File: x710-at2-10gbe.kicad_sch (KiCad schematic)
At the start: 22 parts, among them U4 EZX710AT2_S_LMR5

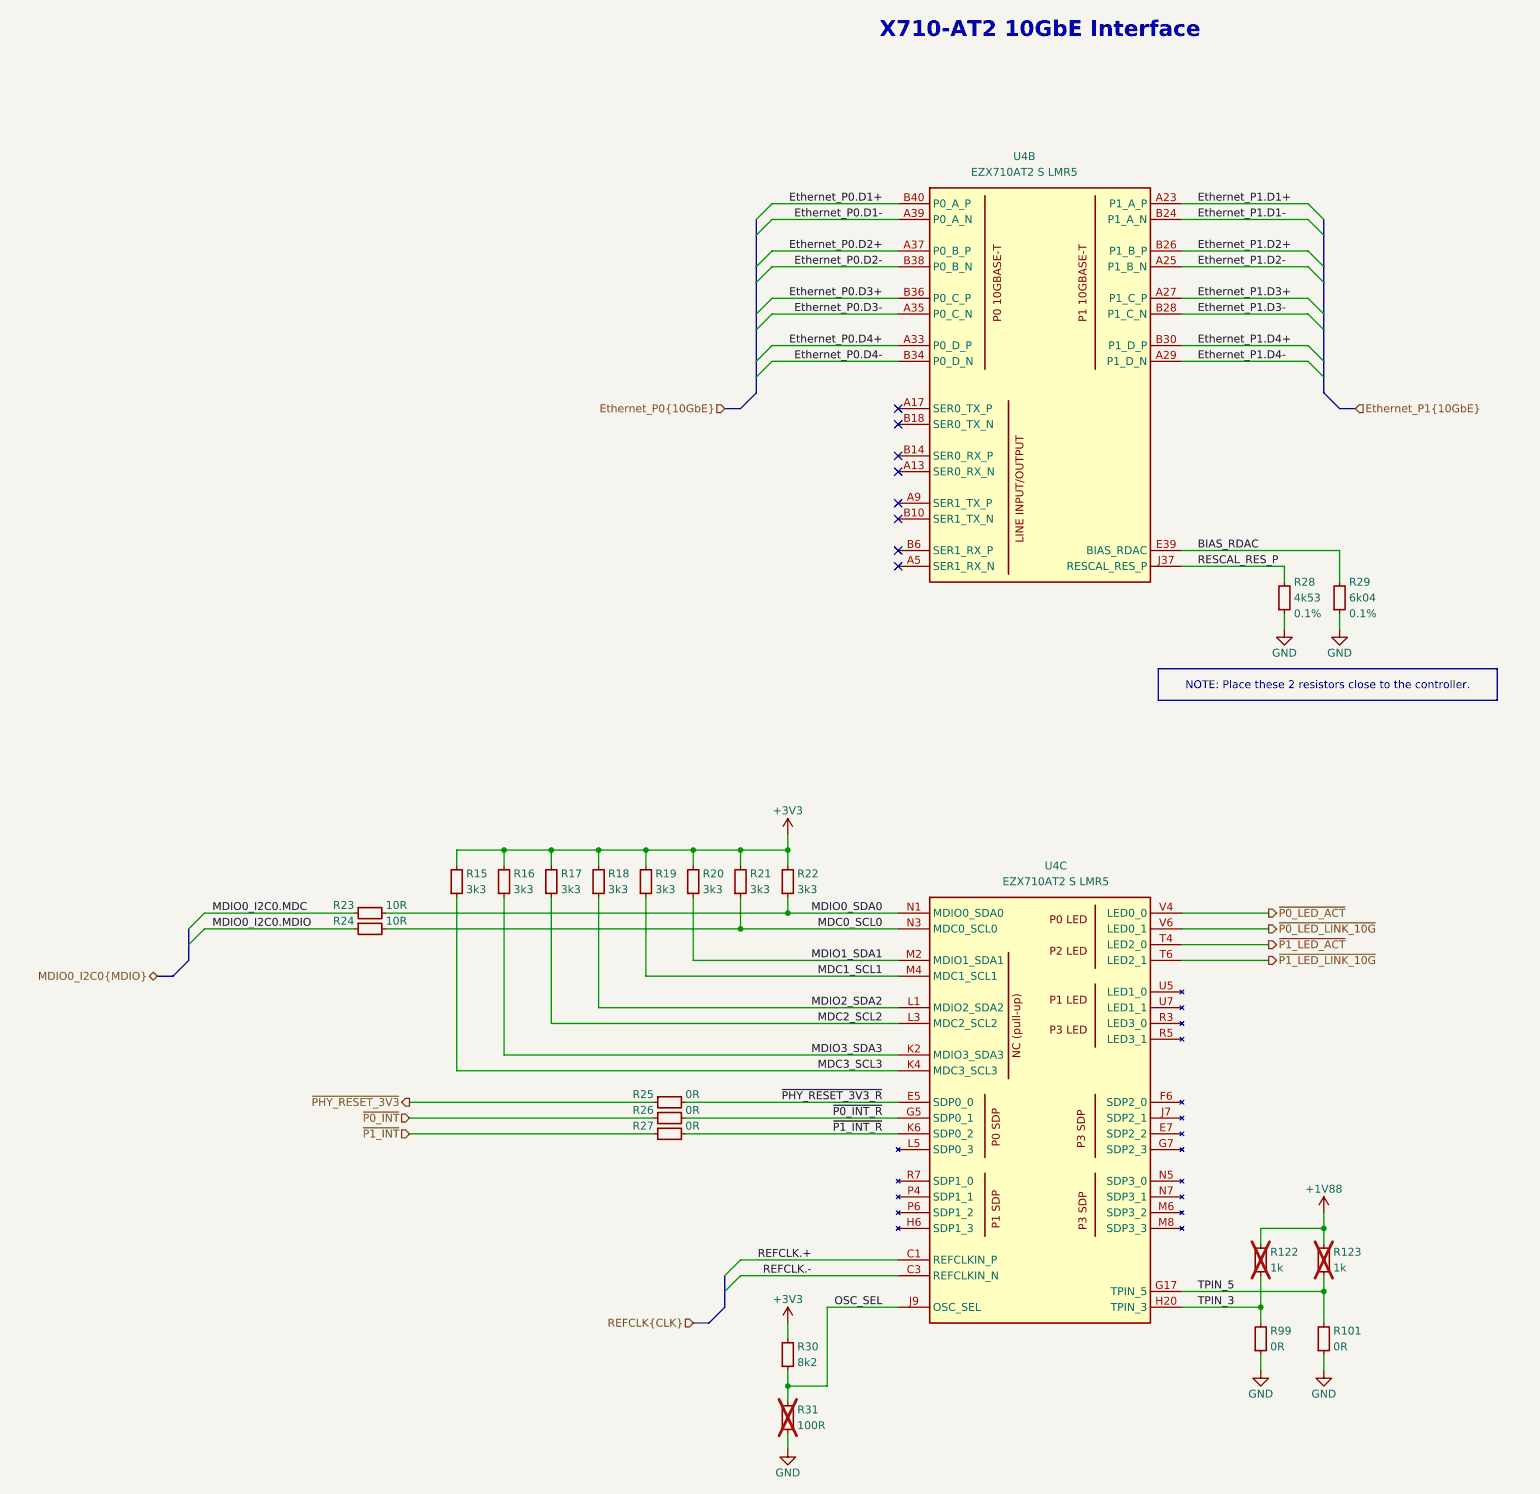
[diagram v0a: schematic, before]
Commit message: [#80813] Add OCuLink connector
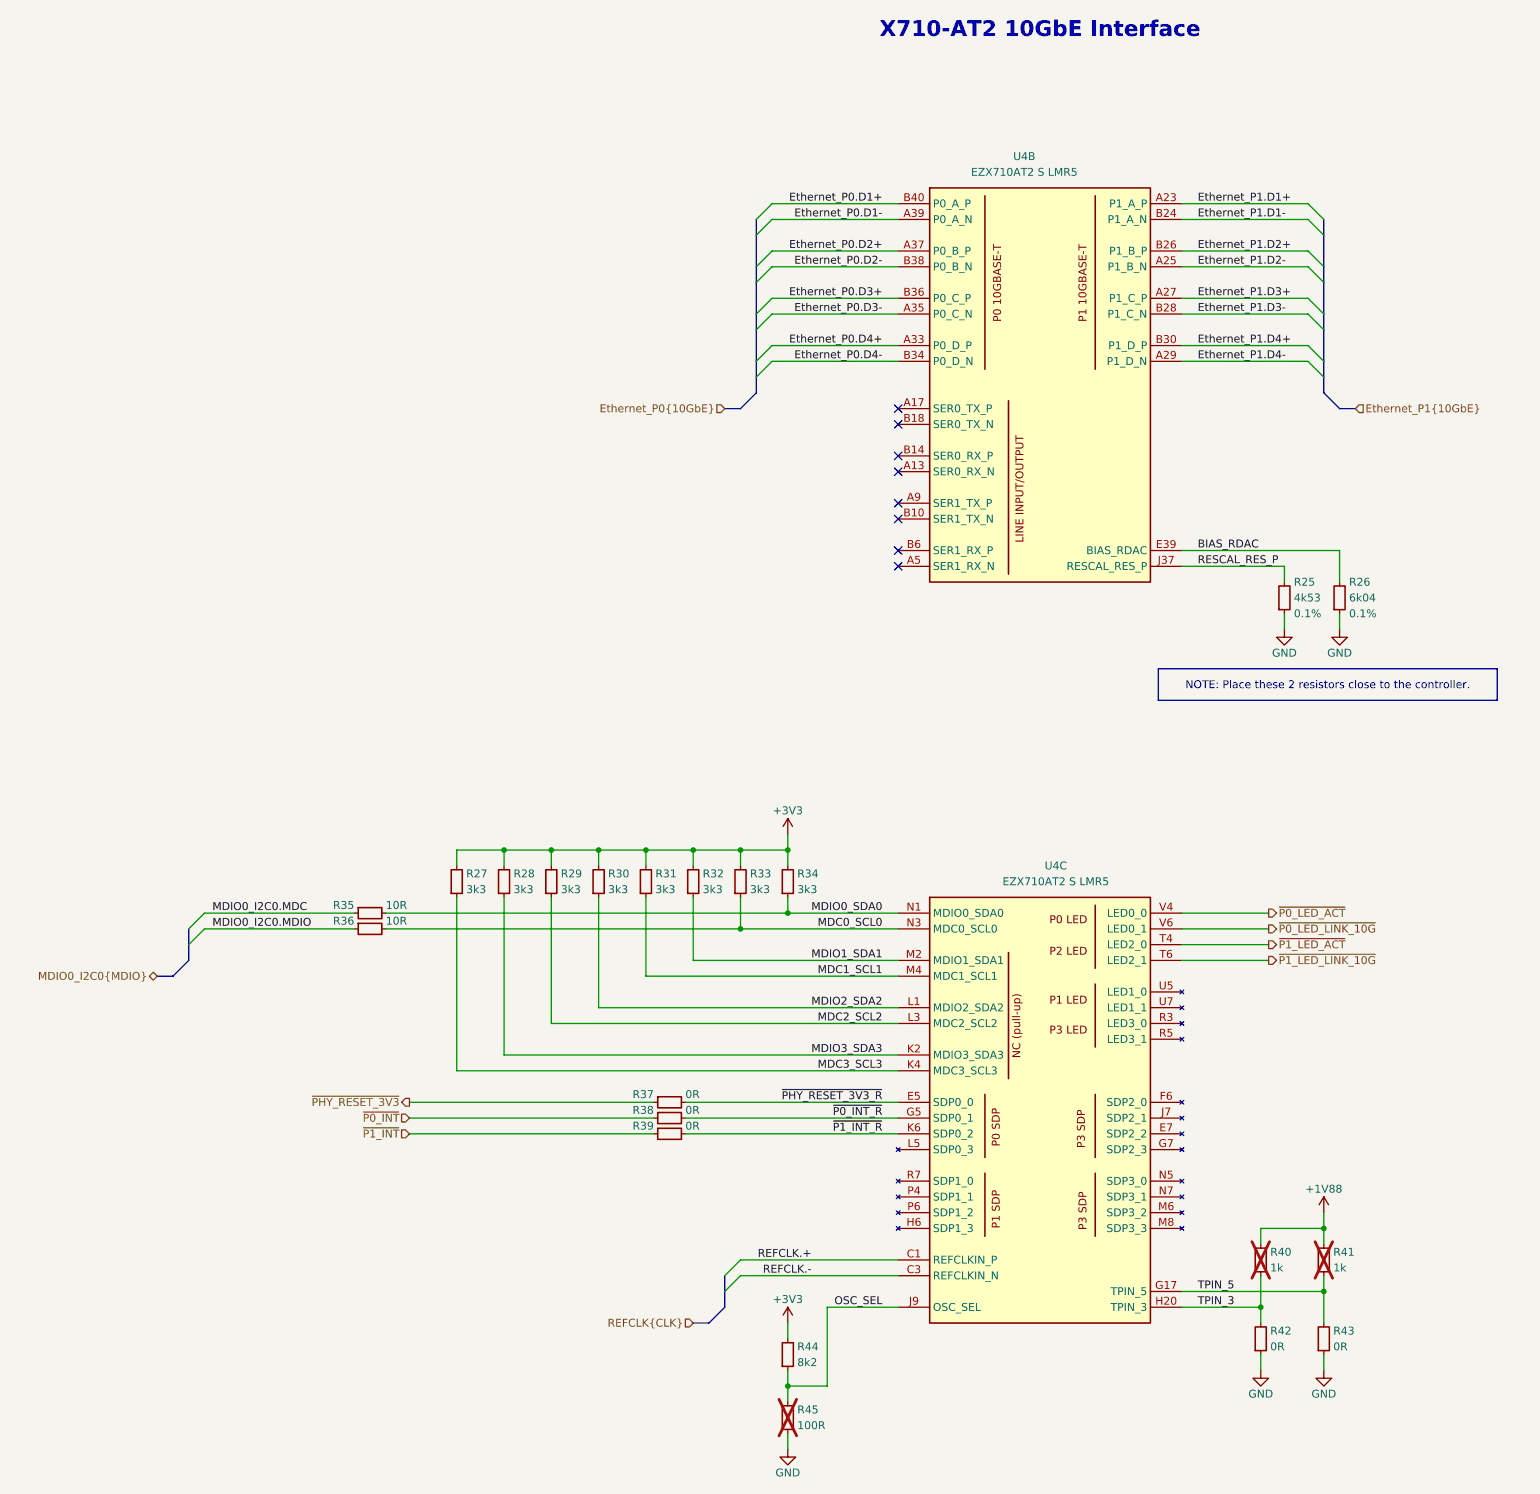
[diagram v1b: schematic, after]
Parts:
- renumbered R28 to R25, R29 to R26, R15 to R27, R16 to R28, R17 to R29, R18 to R30, R19 to R31, R20 to R32, R21 to R33, R22 to R34, R23 to R35, R24 to R36, R25 to R37, R26 to R38, R27 to R39, R122 to R40, R123 to R41, R99 to R42, R101 to R43, R30 to R44, R31 to R45
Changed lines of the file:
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@@
 		(polyline
 			(pts
-				(xy 191.77 49.53) (xy 143.51 49.53) (xy 143.51 88.9) (xy 191.77 88.9)
+				(xy 288.29 49.53) (xy 240.03 49.53) (xy 240.03 88.9) (xy 288.29 88.9)
 			)
 			(stroke
@@
 		(polyline
 			(pts
-				(xy 288.29 49.53) (xy 240.03 49.53) (xy 240.03 88.9) (xy 288.29 88.9)
+				(xy 191.77 49.53) (xy 143.51 49.53) (xy 143.51 88.9) (xy 191.77 88.9)
 			)
 			(stroke
@@
 		(on_board yes)
 		(dnp no)
-		(property "Reference" "#PWR049"
+		(property "Reference" "#PWR0196"
 			(at 273.05 124.46 0)
 			(effects
@@
 			(project "10-gbe-expansion"
 				(path "/04bda987-e5eb-48b4-9e90-d8211dc11b39/46fcd652-659b-4e06-aa16-4947b5e55b68"
-					(reference "#PWR049")
+					(reference "#PWR0196")
 					(unit 1)
 				)
@@
 		(on_board yes)
 		(dnp no)
-		(property "Reference" "R27"
+		(property "Reference" "R39"
 			(at 153.67 201.93 0)
 			(effects
@@
 			(project "10-gbe-expansion"
 				(path "/04bda987-e5eb-48b4-9e90-d8211dc11b39/46fcd652-659b-4e06-aa16-4947b5e55b68"
-					(reference "R27")
+					(reference "R39")
 					(unit 1)
 				)
@@
 		(on_board yes)
 		(dnp no)
-		(property "Reference" "R22"
+		(property "Reference" "R34"
 			(at 176.784 161.29 90)
 			(effects
@@
 			(project "10-gbe-expansion"
 				(path "/04bda987-e5eb-48b4-9e90-d8211dc11b39/46fcd652-659b-4e06-aa16-4947b5e55b68"
-					(reference "R22")
+					(reference "R34")
 					(unit 1)
 				)
@@
 		(on_board yes)
 		(dnp no)
-		(property "Reference" "R30"
+		(property "Reference" "R44"
 			(at 176.784 237.49 90)
 			(effects
@@
 			(project ""
 				(path "/04bda987-e5eb-48b4-9e90-d8211dc11b39/46fcd652-659b-4e06-aa16-4947b5e55b68"
-					(reference "R30")
+					(reference "R44")
 					(unit 1)
 				)
@@
 		(on_board yes)
 		(dnp no)
-		(property "Reference" "#PWR046"
+		(property "Reference" "#PWR0197"
 			(at 190.5 154.94 0)
 			(effects
@@
 			(project "10-gbe-expansion"
 				(path "/04bda987-e5eb-48b4-9e90-d8211dc11b39/46fcd652-659b-4e06-aa16-4947b5e55b68"
-					(reference "#PWR046")
+					(reference "#PWR0197")
 					(unit 1)
 				)
@@
 		(on_board yes)
 		(dnp no)
-		(property "Reference" "R19"
+		(property "Reference" "R31"
 			(at 153.924 161.29 90)
 			(effects
@@
 			(project "10-gbe-expansion"
 				(path "/04bda987-e5eb-48b4-9e90-d8211dc11b39/46fcd652-659b-4e06-aa16-4947b5e55b68"
-					(reference "R19")
+					(reference "R31")
 					(unit 1)
 				)
@@
 		(on_board yes)
 		(dnp no)
-		(property "Reference" "R21"
+		(property "Reference" "R33"
 			(at 169.164 161.29 90)
 			(effects
@@
 			(project "10-gbe-expansion"
 				(path "/04bda987-e5eb-48b4-9e90-d8211dc11b39/46fcd652-659b-4e06-aa16-4947b5e55b68"
-					(reference "R21")
+					(reference "R33")
 					(unit 1)
 				)
@@
 		(on_board yes)
 		(dnp no)
-		(property "Reference" "#PWR0100"
+		(property "Reference" "#PWR0201"
 			(at 270.51 243.84 0)
 			(effects
@@
 			(project "10-gbe-expansion"
 				(path "/04bda987-e5eb-48b4-9e90-d8211dc11b39/46fcd652-659b-4e06-aa16-4947b5e55b68"
-					(reference "#PWR0100")
+					(reference "#PWR0201")
 					(unit 1)
 				)
@@
 		(on_board yes)
 		(dnp no)
-		(property "Reference" "R26"
+		(property "Reference" "R38"
 			(at 153.67 199.39 0)
 			(effects
@@
 			(project "10-gbe-expansion"
 				(path "/04bda987-e5eb-48b4-9e90-d8211dc11b39/46fcd652-659b-4e06-aa16-4947b5e55b68"
-					(reference "R26")
+					(reference "R38")
 					(unit 1)
 				)
@@
 		(on_board yes)
 		(dnp no)
-		(property "Reference" "#PWR047"
+		(property "Reference" "#PWR0199"
 			(at 190.5 233.68 0)
 			(effects
@@
 			(project "10-gbe-expansion"
 				(path "/04bda987-e5eb-48b4-9e90-d8211dc11b39/46fcd652-659b-4e06-aa16-4947b5e55b68"
-					(reference "#PWR047")
+					(reference "#PWR0199")
 					(unit 1)
 				)
@@
 		(on_board yes)
 		(dnp no)
-		(property "Reference" "#PWR048"
+		(property "Reference" "#PWR0195"
 			(at 264.16 124.46 0)
 			(effects
@@
 			(project "10-gbe-expansion"
 				(path "/04bda987-e5eb-48b4-9e90-d8211dc11b39/46fcd652-659b-4e06-aa16-4947b5e55b68"
-					(reference "#PWR048")
+					(reference "#PWR0195")
 					(unit 1)
 				)
@@
 		(on_board yes)
 		(dnp no)
-		(property "Reference" "R24"
+		(property "Reference" "R36"
 			(at 105.41 168.91 0)
 			(effects
@@
 			(project "10-gbe-expansion"
 				(path "/04bda987-e5eb-48b4-9e90-d8211dc11b39/46fcd652-659b-4e06-aa16-4947b5e55b68"
-					(reference "R24")
+					(reference "R36")
 					(unit 1)
 				)
@@
 		(on_board yes)
 		(dnp no)
-		(property "Reference" "#PWR050"
+		(property "Reference" "#PWR0202"
 			(at 184.15 256.54 0)
 			(effects
@@
 			(project "10-gbe-expansion"
 				(path "/04bda987-e5eb-48b4-9e90-d8211dc11b39/46fcd652-659b-4e06-aa16-4947b5e55b68"
-					(reference "#PWR050")
+					(reference "#PWR0202")
 					(unit 1)
 				)
@@
 		(on_board yes)
 		(dnp no)
-		(property "Reference" "R29"
+		(property "Reference" "R26"
 			(at 265.684 114.3 90)
 			(effects
@@
 			(project "10-gbe-expansion"
 				(path "/04bda987-e5eb-48b4-9e90-d8211dc11b39/46fcd652-659b-4e06-aa16-4947b5e55b68"
-					(reference "R29")
+					(reference "R26")
 					(unit 1)
 				)
@@
 		(on_board yes)
 		(dnp no)
-		(property "Reference" "R101"
+		(property "Reference" "R43"
 			(at 263.144 234.95 90)
 			(effects
@@
 			(project "10-gbe-expansion"
 				(path "/04bda987-e5eb-48b4-9e90-d8211dc11b39/46fcd652-659b-4e06-aa16-4947b5e55b68"
-					(reference "R101")
+					(reference "R43")
 					(unit 1)
 				)
@@
 		(on_board yes)
 		(dnp yes)
-		(property "Reference" "R31"
+		(property "Reference" "R45"
 			(at 176.784 247.65 90)
 			(effects
@@
 			(project ""
 				(path "/04bda987-e5eb-48b4-9e90-d8211dc11b39/46fcd652-659b-4e06-aa16-4947b5e55b68"
-					(reference "R31")
+					(reference "R45")
 					(unit 1)
 				)
@@
 		(on_board yes)
 		(dnp no)
-		(property "Reference" "#PWR093"
+		(property "Reference" "#PWR0198"
 			(at 276.86 218.44 0)
 			(effects
@@
 			(project "10-gbe-expansion"
 				(path "/04bda987-e5eb-48b4-9e90-d8211dc11b39/46fcd652-659b-4e06-aa16-4947b5e55b68"
-					(reference "#PWR093")
+					(reference "#PWR0198")
 					(unit 1)
 				)
@@
 		(on_board yes)
 		(dnp no)
-		(property "Reference" "R23"
+		(property "Reference" "R35"
 			(at 105.41 166.37 0)
 			(effects
@@
 			(project ""
 				(path "/04bda987-e5eb-48b4-9e90-d8211dc11b39/46fcd652-659b-4e06-aa16-4947b5e55b68"
-					(reference "R23")
+					(reference "R35")
 					(unit 1)
 				)
@@
 		(on_board yes)
 		(dnp no)
-		(property "Reference" "R18"
+		(property "Reference" "R30"
 			(at 146.304 161.29 90)
 			(effects
@@
 			(project ""
 				(path "/04bda987-e5eb-48b4-9e90-d8211dc11b39/46fcd652-659b-4e06-aa16-4947b5e55b68"
-					(reference "R18")
+					(reference "R30")
 					(unit 1)
 				)
@@
 		(on_board yes)
 		(dnp no)
-		(property "Reference" "R28"
+		(property "Reference" "R25"
 			(at 256.794 114.3 90)
 			(effects
@@
 			(project "10-gbe-expansion"
 				(path "/04bda987-e5eb-48b4-9e90-d8211dc11b39/46fcd652-659b-4e06-aa16-4947b5e55b68"
-					(reference "R28")
+					(reference "R25")
 					(unit 1)
 				)
@@
 		(on_board yes)
 		(dnp no)
-		(property "Reference" "R99"
+		(property "Reference" "R42"
 			(at 252.984 234.95 90)
 			(effects
@@
 			(project "10-gbe-expansion"
 				(path "/04bda987-e5eb-48b4-9e90-d8211dc11b39/46fcd652-659b-4e06-aa16-4947b5e55b68"
-					(reference "R99")
+					(reference "R42")
 					(unit 1)
 				)
@@
 		(on_board yes)
 		(dnp no)
-		(property "Reference" "R17"
+		(property "Reference" "R29"
 			(at 138.684 161.29 90)
 			(effects
@@
 			(project "10-gbe-expansion"
 				(path "/04bda987-e5eb-48b4-9e90-d8211dc11b39/46fcd652-659b-4e06-aa16-4947b5e55b68"
-					(reference "R17")
+					(reference "R29")
 					(unit 1)
 				)
@@
 		(on_board yes)
 		(dnp yes)
-		(property "Reference" "R122"
+		(property "Reference" "R40"
 			(at 252.984 222.25 90)
 			(effects
@@
 			(project "10-gbe-expansion"
 				(path "/04bda987-e5eb-48b4-9e90-d8211dc11b39/46fcd652-659b-4e06-aa16-4947b5e55b68"
-					(reference "R122")
+					(reference "R40")
 					(unit 1)
 				)
@@
 		(on_board yes)
 		(dnp no)
-		(property "Reference" "#PWR098"
+		(property "Reference" "#PWR0200"
 			(at 260.35 243.84 0)
 			(effects
@@
 			(project "10-gbe-expansion"
 				(path "/04bda987-e5eb-48b4-9e90-d8211dc11b39/46fcd652-659b-4e06-aa16-4947b5e55b68"
-					(reference "#PWR098")
+					(reference "#PWR0200")
 					(unit 1)
 				)
@@
 		(on_board yes)
 		(dnp no)
-		(property "Reference" "R16"
+		(property "Reference" "R28"
 			(at 131.064 161.29 90)
 			(effects
@@
 			(project "10-gbe-expansion"
 				(path "/04bda987-e5eb-48b4-9e90-d8211dc11b39/46fcd652-659b-4e06-aa16-4947b5e55b68"
-					(reference "R16")
+					(reference "R28")
 					(unit 1)
 				)
@@
 		(on_board yes)
 		(dnp no)
-		(property "Reference" "R15"
+		(property "Reference" "R27"
 			(at 123.444 161.29 90)
 			(effects
@@
 			(project "10-gbe-expansion"
 				(path "/04bda987-e5eb-48b4-9e90-d8211dc11b39/46fcd652-659b-4e06-aa16-4947b5e55b68"
-					(reference "R15")
+					(reference "R27")
 					(unit 1)
 				)
@@
 		(on_board yes)
 		(dnp no)
-		(property "Reference" "R20"
+		(property "Reference" "R32"
 			(at 161.544 161.29 90)
 			(effects
@@
 			(project "10-gbe-expansion"
 				(path "/04bda987-e5eb-48b4-9e90-d8211dc11b39/46fcd652-659b-4e06-aa16-4947b5e55b68"
-					(reference "R20")
+					(reference "R32")
 					(unit 1)
 				)
@@
 		(on_board yes)
 		(dnp no)
-		(property "Reference" "R25"
+		(property "Reference" "R37"
 			(at 153.67 196.85 0)
 			(effects
@@
 			(project ""
 				(path "/04bda987-e5eb-48b4-9e90-d8211dc11b39/46fcd652-659b-4e06-aa16-4947b5e55b68"
-					(reference "R25")
+					(reference "R37")
 					(unit 1)
 				)
@@
 		(on_board yes)
 		(dnp yes)
-		(property "Reference" "R123"
+		(property "Reference" "R41"
 			(at 263.144 222.25 90)
 			(effects
@@
 			(project "10-gbe-expansion"
 				(path "/04bda987-e5eb-48b4-9e90-d8211dc11b39/46fcd652-659b-4e06-aa16-4947b5e55b68"
-					(reference "R123")
+					(reference "R41")
 					(unit 1)
 				)

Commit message: [#80813] Add power input connectors, heatsink, mounting, draft component placement
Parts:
- R40, R41, R45: now left out of the parts list
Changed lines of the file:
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@@
 		(polyline
 			(pts
-				(xy 288.29 49.53) (xy 240.03 49.53) (xy 240.03 88.9) (xy 288.29 88.9)
+				(xy 191.77 49.53) (xy 143.51 49.53) (xy 143.51 88.9) (xy 191.77 88.9)
 			)
 			(stroke
@@
 		(polyline
 			(pts
-				(xy 191.77 49.53) (xy 143.51 49.53) (xy 143.51 88.9) (xy 191.77 88.9)
+				(xy 288.29 49.53) (xy 240.03 49.53) (xy 240.03 88.9) (xy 288.29 88.9)
 			)
 			(stroke
@@
 		(unit 1)
 		(exclude_from_sim no)
-		(in_bom yes)
+		(in_bom no)
 		(on_board yes)
 		(dnp yes)
@@
 		(unit 1)
 		(exclude_from_sim no)
-		(in_bom yes)
+		(in_bom no)
 		(on_board yes)
 		(dnp yes)
@@
 		(unit 1)
 		(exclude_from_sim no)
-		(in_bom yes)
+		(in_bom no)
 		(on_board yes)
 		(dnp yes)

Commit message: [#81595] Update symbols from library
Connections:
- no-connect marks 8 -> 25
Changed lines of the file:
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@@
 	)
 	(no_connect
+		(at 238.76 213.36)
+	)
+	(no_connect
+		(at 238.76 200.66)
+	)
+	(no_connect
+		(at 238.76 180.34)
+	)
+	(no_connect
+		(at 238.76 182.88)
+	)
+	(no_connect
+		(at 193.04 218.44)
+	)
+	(no_connect
+		(at 238.76 215.9)
+	)
+	(no_connect
 		(at 193.04 88.9)
 	)
 	(no_connect
+		(at 193.04 210.82)
+	)
+	(no_connect
+		(at 238.76 187.96)
+	)
+	(no_connect
 		(at 193.04 86.36)
 	)
 	(no_connect
+		(at 193.04 213.36)
+	)
+	(no_connect
+		(at 238.76 203.2)
+	)
+	(no_connect
+		(at 238.76 198.12)
+	)
+	(no_connect
+		(at 193.04 205.74)
+	)
+	(no_connect
+		(at 238.76 210.82)
+	)
+	(no_connect
 		(at 193.04 109.22)
 	)
@@
 	)
 	(no_connect
+		(at 193.04 215.9)
+	)
+	(no_connect
 		(at 193.04 96.52)
 	)
+	(no_connect
+		(at 238.76 205.74)
+	)
+	(no_connect
+		(at 238.76 218.44)
+	)
+	(no_connect
+		(at 238.76 185.42)
+	)
 	(bus_entry
 		(at 165.1 228.6)
@@
 		(pin "N27"
 		)
-		(pin "M15"
-		)
-		(pin "M31"
+		(pin "V34"
 		)
 		(pin "L7"
@@
 	)
 	(symbol
-		(lib_name "EZX710AT2_S_LMR5_1")
 		(lib_id "antmicroInterfaceControllers:EZX710AT2_S_LMR5")
 		(at 193.04 167.64 0)
